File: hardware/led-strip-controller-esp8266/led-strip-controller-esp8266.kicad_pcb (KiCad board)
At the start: 2 copper layers, 24 parts, among them J1 Conn_01x15_Female, J2 Conn_01x05_Female, Q1 IRLZ44N, Q10 IRLZ44N, Q11 IRLZ44N, Q12 IRLZ44N, Q2 IRLZ44N, Q3 IRLZ44N, Q4 IRLZ44N, Q5 IRLZ44N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

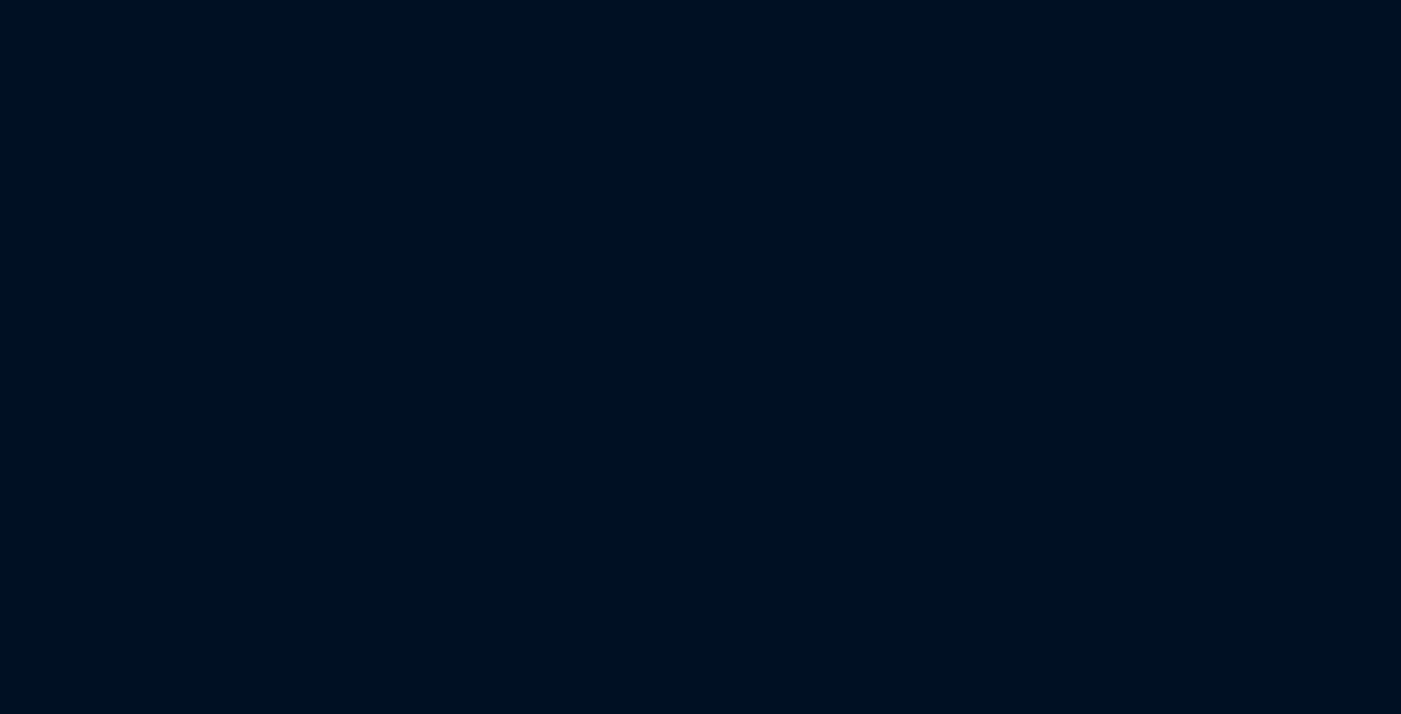
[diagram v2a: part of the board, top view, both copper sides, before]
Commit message: Add power supply module and power jack.
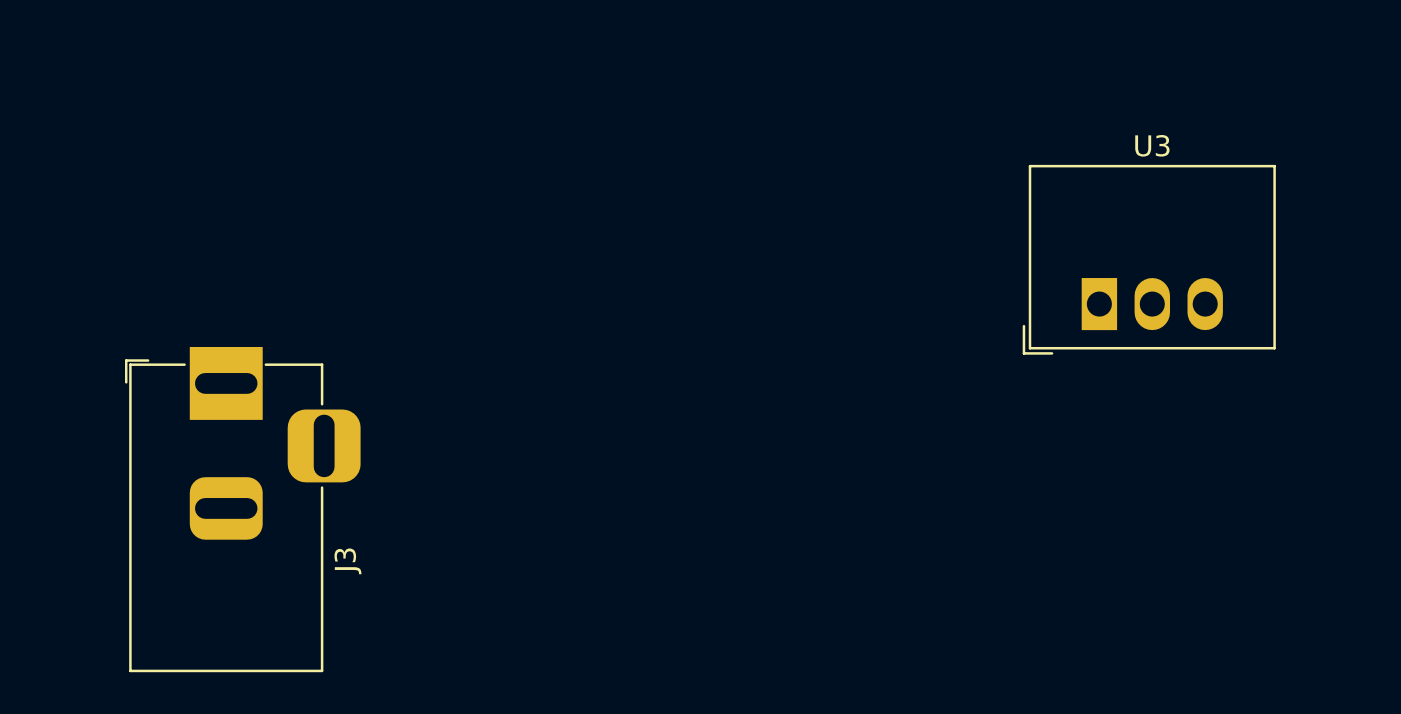
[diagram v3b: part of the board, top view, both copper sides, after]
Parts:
- added J3: Barrel_Jack, Connector_BarrelJack:BarrelJack_Horizontal, F.Cu at (96.5, 132.1)
- added U3: R-78HB3.3-0.5, Converter_DCDC:Converter_DCDC_RECOM_R-78HB-0.5_THT, F.Cu at (138.4, 128.3)
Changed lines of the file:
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@@
     (tracks 0)
     (zones 0)
-    (modules 24)
-    (nets 47)
+    (modules 26)
+    (nets 48)
   )
   (page A4)
@@
   (net 45 "Net-(U2-Pad8)")
   (net 46 /RESET)
+  (net 47 "Net-(J3-Pad3)")
   (net_class Default "This is the default net class."
     (clearance 0.2)
@@
     (add_net GND)
     (add_net "Net-(C1-Pad1)")
+    (add_net "Net-(J3-Pad3)")
     (add_net "Net-(R3-Pad1)")
     (add_net "Net-(U1-Pad10)")
@@
     (add_net "Net-(U2-Pad8)")
   )
+  (module Connector_BarrelJack:BarrelJack_Horizontal (layer F.Cu)
+    (at 96.52 132.08 90)
+    (descr "DC Barrel Jack")
+    (tags "Power Jack")
+    (fp_text reference J3 (at -8.45 5.75 90) (layer F.SilkS)
+      (effects (font (size 1 1) (thickness 0.15)))
+    )
+    (fp_text value Barrel_Jack (at -6.2 -5.5 90) (layer F.Fab)
+      (effects (font (size 1 1) (thickness 0.15)))
+    )
+    (fp_text user %R (at -3 -2.95 90) (layer F.Fab)
+      (effects (font (size 1 1) (thickness 0.15)))
+    )
+    (fp_line (start -0.003213 -4.505425) (end 0.8 -3.75) (layer F.Fab) (width 0.1))
+    (fp_line (start 1.1 -3.75) (end 1.1 -4.8) (layer F.SilkS) (width 0.12))
+    (fp_line (start 0.05 -4.8) (end 1.1 -4.8) (layer F.SilkS) (width 0.12))
+    (fp_line (start 1 -4.5) (end 1 -4.75) (layer F.CrtYd) (width 0.05))
+    (fp_line (start 1 -4.75) (end -14 -4.75) (layer F.CrtYd) (width 0.05))
+    (fp_line (start 1 -4.5) (end 1 -2) (layer F.CrtYd) (width 0.05))
+    (fp_line (start 1 -2) (end 2 -2) (layer F.CrtYd) (width 0.05))
+    (fp_line (start 2 -2) (end 2 2) (layer F.CrtYd) (width 0.05))
+    (fp_line (start 2 2) (end 1 2) (layer F.CrtYd) (width 0.05))
+    (fp_line (start 1 2) (end 1 4.75) (layer F.CrtYd) (width 0.05))
+    (fp_line (start 1 4.75) (end -1 4.75) (layer F.CrtYd) (width 0.05))
+    (fp_line (start -1 4.75) (end -1 6.75) (layer F.CrtYd) (width 0.05))
+    (fp_line (start -1 6.75) (end -5 6.75) (layer F.CrtYd) (width 0.05))
+    (fp_line (start -5 6.75) (end -5 4.75) (layer F.CrtYd) (width 0.05))
+    (fp_line (start -5 4.75) (end -14 4.75) (layer F.CrtYd) (width 0.05))
+    (fp_line (start -14 4.75) (end -14 -4.75) (layer F.CrtYd) (width 0.05))
+    (fp_line (start -5 4.6) (end -13.8 4.6) (layer F.SilkS) (width 0.12))
+    (fp_line (start -13.8 4.6) (end -13.8 -4.6) (layer F.SilkS) (width 0.12))
+    (fp_line (start 0.9 1.9) (end 0.9 4.6) (layer F.SilkS) (width 0.12))
+    (fp_line (start 0.9 4.6) (end -1 4.6) (layer F.SilkS) (width 0.12))
+    (fp_line (start -13.8 -4.6) (end 0.9 -4.6) (layer F.SilkS) (width 0.12))
+    (fp_line (start 0.9 -4.6) (end 0.9 -2) (layer F.SilkS) (width 0.12))
+    (fp_line (start -10.2 -4.5) (end -10.2 4.5) (layer F.Fab) (width 0.1))
+    (fp_line (start -13.7 -4.5) (end -13.7 4.5) (layer F.Fab) (width 0.1))
+    (fp_line (start -13.7 4.5) (end 0.8 4.5) (layer F.Fab) (width 0.1))
+    (fp_line (start 0.8 4.5) (end 0.8 -3.75) (layer F.Fab) (width 0.1))
+    (fp_line (start 0 -4.5) (end -13.7 -4.5) (layer F.Fab) (width 0.1))
+    (pad 1 thru_hole rect (at 0 0 90) (size 3.5 3.5) (drill oval 1 3) (layers *.Cu *.Mask)
+      (net 12 +12V))
+    (pad 2 thru_hole roundrect (at -6 0 90) (size 3 3.5) (drill oval 1 3) (layers *.Cu *.Mask) (roundrect_rratio 0.25)
+      (net 1 GND))
+    (pad 3 thru_hole roundrect (at -3 4.7 90) (size 3.5 3.5) (drill oval 3 1) (layers *.Cu *.Mask) (roundrect_rratio 0.25)
+      (net 47 "Net-(J3-Pad3)"))
+    (model ${KISYS3DMOD}/Connector_BarrelJack.3dshapes/BarrelJack_Horizontal.wrl
+      (at (xyz 0 0 0))
+      (scale (xyz 1 1 1))
+      (rotate (xyz 0 0 0))
+    )
+  )
+  (module Converter_DCDC:Converter_DCDC_RECOM_R-78HB-0.5_THT (layer F.Cu)
+    (at 138.43 128.27)
+    (descr "DCDC-Converter, RECOM, RECOM_R-78HB-0.5, SIP-3, pitch 2.54mm, package size 11.5x8.5x17.5mm^3, https://www.recom-power.com/pdf/Innoline/R-78HBxx-0.5_L.pdf")
+    (tags "dc-dc recom buck sip-3 pitch 2.54mm")
+    (fp_text reference U3 (at 2.54 -7.56) (layer F.SilkS)
+      (effects (font (size 1 1) (thickness 0.15)))
+    )
+    (fp_text value R-78HB3.3-0.5 (at 2.42 3.42) (layer F.Fab)
+      (effects (font (size 1 1) (thickness 0.15)))
+    )
+    (fp_line (start -3.21 -6.5) (end 8.29 -6.5) (layer F.Fab) (width 0.1))
+    (fp_line (start 8.29 -6.5) (end 8.29 2) (layer F.Fab) (width 0.1))
+    (fp_line (start 8.29 2) (end -2.21 2) (layer F.Fab) (width 0.1))
+    (fp_line (start -2.21 2) (end -3.21 1) (layer F.Fab) (width 0.1))
+    (fp_line (start -3.21 1) (end -3.21 -6.5) (layer F.Fab) (width 0.1))
+    (fp_line (start -3.33 -6.62) (end 8.41 -6.62) (layer F.SilkS) (width 0.12))
+    (fp_line (start -3.33 2.12) (end 8.41 2.12) (layer F.SilkS) (width 0.12))
+    (fp_line (start -3.33 -6.62) (end -3.33 2.12) (layer F.SilkS) (width 0.12))
+    (fp_line (start 8.41 -6.62) (end 8.41 2.12) (layer F.SilkS) (width 0.12))
+    (fp_line (start -3.62 1.06) (end -3.62 2.37) (layer F.SilkS) (width 0.12))
+    (fp_line (start -3.62 2.37) (end -2.27 2.37) (layer F.SilkS) (width 0.12))
+    (fp_line (start -3.5 -6.75) (end -3.5 2.25) (layer F.CrtYd) (width 0.05))
+    (fp_line (start -3.5 2.25) (end 8.55 2.25) (layer F.CrtYd) (width 0.05))
+    (fp_line (start 8.55 2.25) (end 8.55 -6.75) (layer F.CrtYd) (width 0.05))
+    (fp_line (start 8.55 -6.75) (end -3.5 -6.75) (layer F.CrtYd) (width 0.05))
+    (fp_text user %R (at 2.54 -2.25) (layer F.Fab)
+      (effects (font (size 1 1) (thickness 0.15)))
+    )
+    (pad 1 thru_hole rect (at 0 0) (size 1.7 2.5) (drill 1.2) (layers *.Cu *.Mask)
+      (net 12 +12V))
+    (pad 2 thru_hole oval (at 2.54 0) (size 1.7 2.5) (drill 1.2) (layers *.Cu *.Mask)
+      (net 1 GND))
+    (pad 3 thru_hole oval (at 5.08 0) (size 1.7 2.5) (drill 1.2) (layers *.Cu *.Mask)
+      (net 4 +3V3))
+    (model ${KISYS3DMOD}/Converter_DCDC.3dshapes/Converter_DCDC_RECOM_R-78HB-0.5_THT.wrl
+      (at (xyz 0 0 0))
+      (scale (xyz 1 1 1))
+      (rotate (xyz 0 0 0))
+    )
+  )
   (module Connector_Pin:Pin_D1.0mm_L10.0mm (layer F.Cu)

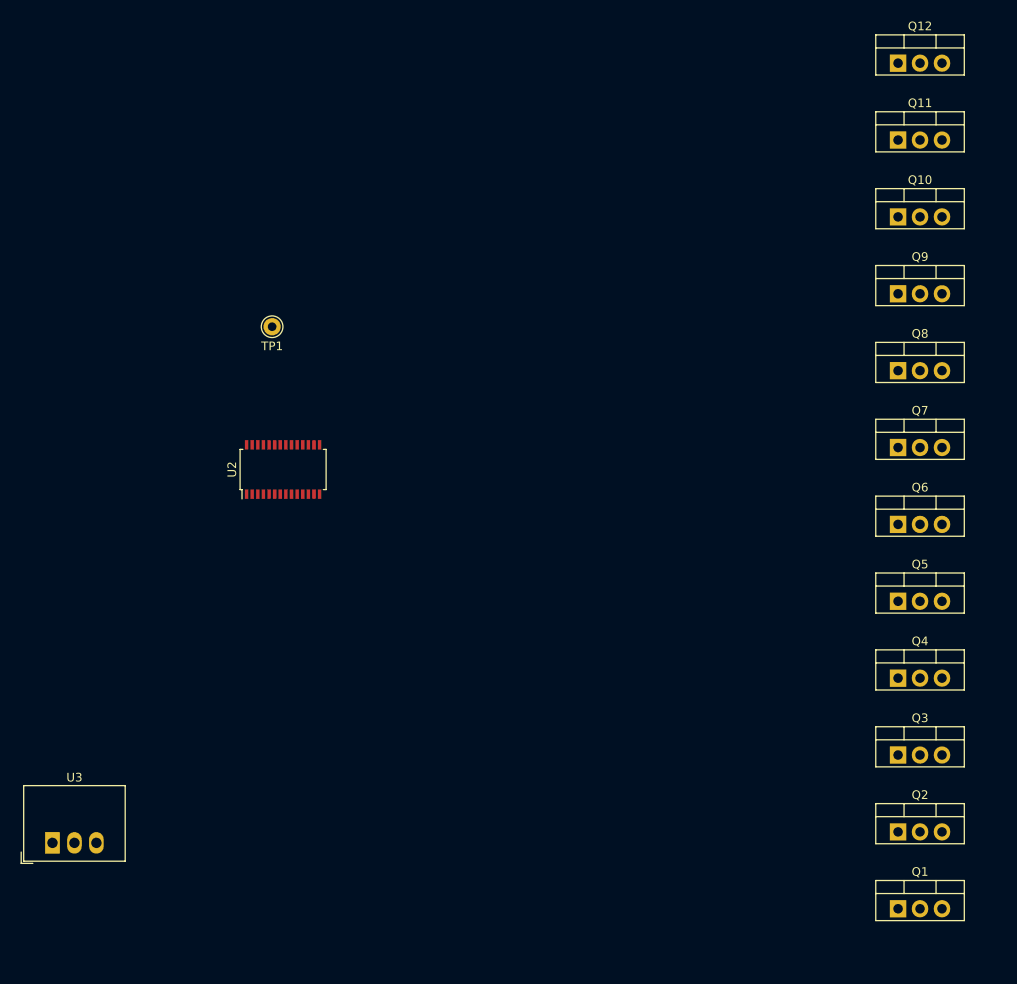
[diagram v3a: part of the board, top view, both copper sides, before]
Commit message: Add TVS diode and new MOSFET array to schematic.
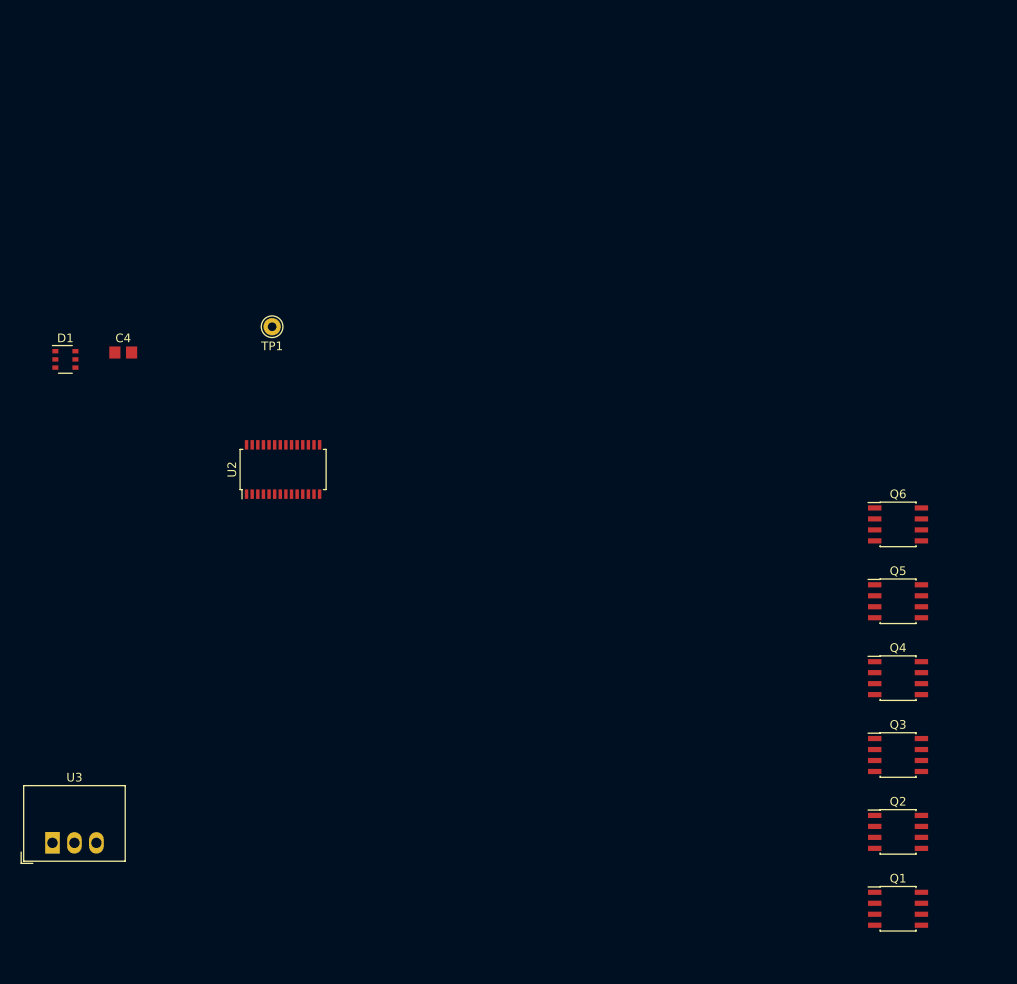
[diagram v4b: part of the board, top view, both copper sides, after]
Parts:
- removed Q10, Q11, Q12, Q7, Q8, Q9: IRLZ44N, Package_TO_SOT_THT:TO-220-3_Vertical
- added C4: 0.1uF, Capacitor_SMD:C_0805_2012Metric_Pad1.29x1.40mm_HandSolder, F.Cu at (146.6, 71.6)
- added D1: TVS3V3L4U, Package_SO:TSOP-6_1.65x3.05mm_P0.95mm, F.Cu at (139.9, 72.4)
- Q1, Q2, Q3, Q4, Q5, Q6: value IRLZ44N -> DMN3018SSD; footprint Package_TO_SOT_THT:TO-220-3_Vertical -> Package_SO:SOIC-8_3.9x4.9mm_P1.27mm
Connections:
- Q1 pad 1: /LED_PWM1 -> GND
- Q1 pad 2: /LED Strips/LED1 -> /LED_PWM1
- Q2 pad 1: /LED_PWM2 -> GND
- Q2 pad 2: /LED Strips/LED2 -> /LED_PWM1
- Q3 pad 1: /LED_PWM3 -> GND
- Q3 pad 2: /LED Strips/LED3 -> /LED_PWM1
- Q4 pad 1: /LED_PWM4 -> GND
- Q4 pad 2: /LED Strips/LED4 -> /LED_PWM1
- Q5 pad 1: /LED_PWM5 -> GND
- Q5 pad 2: /LED Strips/LED5 -> /LED_PWM1
- Q6 pad 1: /LED_PWM6 -> GND
- Q6 pad 2: /LED Strips/LED6 -> /LED_PWM1
- U2 pad 11: /LED_PWM3 -> /LED_PWM1
- U2 pad 13: /LED_PWM5 -> /LED_PWM1
- U2 pad 16: /LED_PWM7 -> /LED_PWM1
- U2 pad 18: /LED_PWM9 -> /LED_PWM1
- U2 pad 20: /LED_PWM11 -> /LED_PWM1

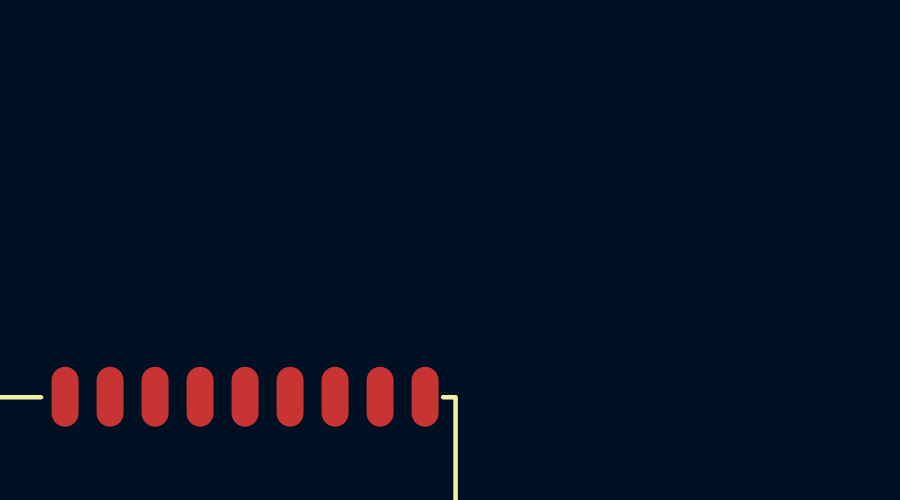
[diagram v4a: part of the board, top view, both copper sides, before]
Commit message: Add status LED and resistor.
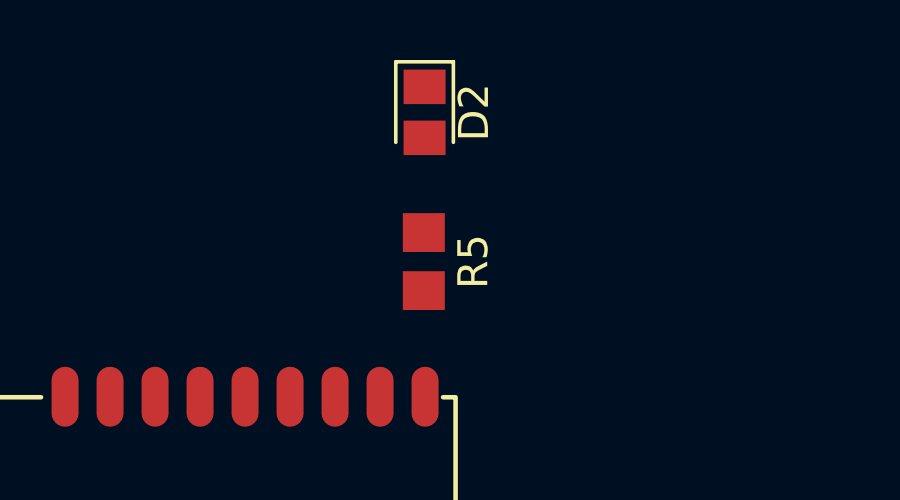
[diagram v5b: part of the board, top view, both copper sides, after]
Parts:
- added D2: LED, LED_SMD:LED_0805_2012Metric, F.Cu at (63.9, 64.6)
- added R5: 470, Resistor_SMD:R_0805_2012Metric_Pad1.29x1.40mm_HandSolder, F.Cu at (63.9, 69.6)
